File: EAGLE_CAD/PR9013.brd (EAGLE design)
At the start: 70 x 70 mm, 55 parts, among them J1 M3_SCREW_POST, Y1 32.768kHz

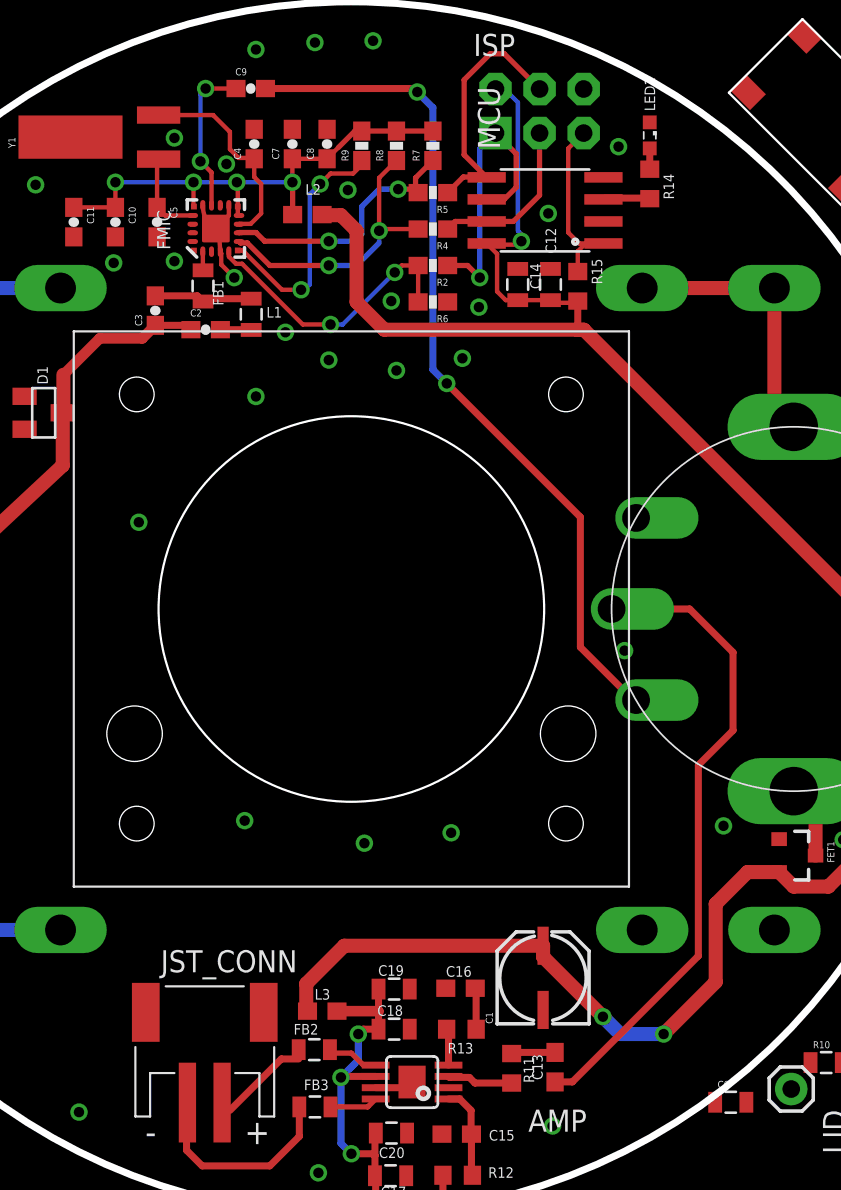
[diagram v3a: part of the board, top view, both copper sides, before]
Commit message: added package variant for speaker
…and replaced the speaker with the variant. this one has no cutout,
just a restrict on both top and bottom layers.
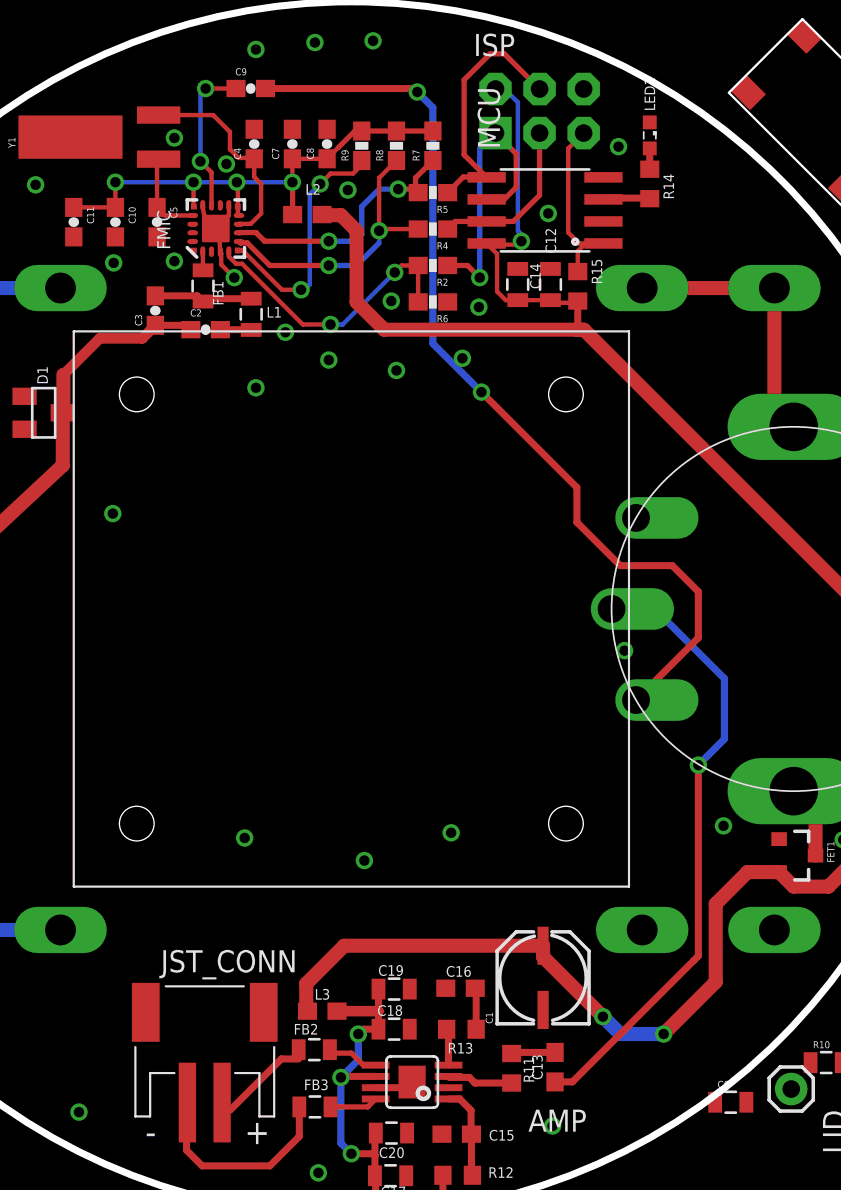
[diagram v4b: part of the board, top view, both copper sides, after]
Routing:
- net A_IN: track 49.2 -> 53.8 mm
- net A_OUT: track 37.6 -> 36.0 mm, vias 0 -> 1
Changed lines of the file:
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@@
 <wire x1="27.44" y1="55.597" x2="27.39" y2="56.447" width="0.254" layer="1"/>
 <wire x1="27.39" y1="56.447" x2="27.19" y2="56.932" width="0.254" layer="1"/>
-<via x="22.75" y="40" extent="1-16" drill="0.6"/>
+<via x="21.25" y="40.5" extent="1-16" drill="0.6"/>
 <via x="36.25" y="67.75" extent="1-16" drill="0.6"/>
 <via x="66.65" y="44.2" extent="1-16" drill="0.6"/>
@@
 <via x="37.6" y="48.75" extent="1-16" drill="0.6"/>
 <via x="21.3" y="54.95" extent="1-16" drill="0.6"/>
-<via x="29.5" y="47.25" extent="1-16" drill="0.6"/>
+<via x="29.5" y="47.75" extent="1-16" drill="0.6"/>
 <via x="16.8" y="59.45" extent="1-16" drill="0.6"/>
 <via x="50.4" y="61.65" extent="1-16" drill="0.6"/>
@@
 <via x="19.3" y="6" extent="1-16" drill="0.6"/>
 <via x="11.1" y="12.7" extent="1-16" drill="0.6"/>
-<via x="28.85" y="22.8" extent="1-16" drill="0.6"/>
-<via x="35.75" y="21.5" extent="1-16" drill="0.6"/>
+<via x="28.85" y="21.8" extent="1-16" drill="0.6"/>
+<via x="35.75" y="20.5" extent="1-16" drill="0.6"/>
 <via x="37.3" y="52.75" extent="1-16" drill="0.6"/>
 <via x="34.8" y="59.15" extent="1-16" drill="0.6"/>
@@
 <via x="24.8" y="62.15" extent="1-16" drill="0.6"/>
 <contactref element="U$1" pad="P$1"/>
-<wire x1="66.65" y1="44.2" x2="61.14141875" y2="68.01005" width="0" layer="19" extent="1-1"/>
+<wire x1="52.2" y1="63.05" x2="61.14141875" y2="68.01005" width="0" layer="19" extent="1-1"/>
 <wire x1="27.2" y1="56.95" x2="27.19" y2="56.932" width="0" layer="19" extent="1-1"/>
 <wire x1="38.16" y1="2.332" x2="33.1" y2="2.5" width="0" layer="19" extent="1-1"/>
@@
 <contactref element="C13" pad="1"/>
 <wire x1="46.74" y1="7.74" x2="47.74" y2="7.74" width="0.4064" layer="1"/>
-<wire x1="47.74" y1="7.74" x2="55" y2="15" width="0.4064" layer="1"/>
-<wire x1="55" y1="15" x2="55" y2="26" width="0.4064" layer="1"/>
-<wire x1="55" y1="26" x2="57" y2="28" width="0.4064" layer="1"/>
-<wire x1="57" y1="28" x2="57" y2="32.5" width="0.4064" layer="1"/>
-<wire x1="57" y1="32.5" x2="54.5" y2="35" width="0.4064" layer="1"/>
-<wire x1="54.5" y1="35" x2="50" y2="35" width="0.4064" layer="1"/>
+<wire x1="47.74" y1="7.74" x2="54.75" y2="14.75" width="0.4064" layer="1"/>
+<wire x1="50" y1="35" x2="52.5" y2="35" width="0.4064" layer="16"/>
+<wire x1="52.5" y1="35" x2="56.5" y2="31" width="0.4064" layer="16"/>
+<wire x1="56.5" y1="31" x2="56.5" y2="27.5" width="0.4064" layer="16"/>
+<wire x1="56.5" y1="27.5" x2="55" y2="26" width="0.4064" layer="16"/>
+<via x="55" y="26" extent="1-16" drill="0.6"/>
+<wire x1="55" y1="26" x2="55" y2="15" width="0.4064" layer="1"/>
+<wire x1="55" y1="15" x2="54.75" y2="14.75" width="0.4064" layer="1"/>
 </signal>
 <signal name="N$23">
@@
 <via x="38.8" y="64.8" extent="1-16" drill="0.6"/>
 <wire x1="38.8" y1="64.8" x2="39.7" y2="63.9" width="0.4064" layer="16"/>
-<wire x1="39.7" y1="63.9" x2="39.7" y2="48.8" width="0.4064" layer="16"/>
-<wire x1="39.7" y1="48.8" x2="40.5" y2="48" width="0.4064" layer="16"/>
-<via x="40.5" y="48" extent="1-16" drill="0.6"/>
-<wire x1="40.5" y1="48" x2="48.2" y2="40.3" width="0.4064" layer="1"/>
-<wire x1="48.2" y1="40.3" x2="48.2" y2="32.8" width="0.4064" layer="1"/>
-<wire x1="48.2" y1="32.8" x2="51.25" y2="29.75" width="0.4064" layer="1"/>
-<wire x1="51.25" y1="29.75" x2="51.41" y2="29.75" width="0.4064" layer="1"/>
+<wire x1="51.41" y1="29.75" x2="55" y2="33.34" width="0.4064" layer="1"/>
+<wire x1="48" y1="40" x2="48" y2="42" width="0.4064" layer="1"/>
+<wire x1="48" y1="42" x2="42.5" y2="47.5" width="0.4064" layer="1"/>
+<via x="42.5" y="47.5" extent="1-16" drill="0.6"/>
+<wire x1="42.5" y1="47.5" x2="39.7" y2="50.3" width="0.4064" layer="16"/>
+<wire x1="39.7" y1="50.3" x2="39.7" y2="63.9" width="0.4064" layer="16"/>
+<wire x1="50.5" y1="37.5" x2="53.5" y2="37.5" width="0.4064" layer="1"/>
+<wire x1="53.5" y1="37.5" x2="55" y2="36" width="0.4064" layer="1"/>
+<wire x1="55" y1="36" x2="55" y2="33.34" width="0.4064" layer="1"/>
+<wire x1="48" y1="40" x2="50.5" y2="37.5" width="0.4064" layer="1"/>
 </signal>
 <signal name="N$3">
